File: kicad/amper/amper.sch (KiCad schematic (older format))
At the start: 59 parts, among them J1 Conn_02x05_Odd_Even, J2 Conn_02x05_Odd_Even, J3 Conn_02x05_Odd_Even, J4 USB_C_Receptacle_USB2.0, J5 Conn_01x03, J6 Conn_01x04, J7 Conn_01x05, J8 Conn_01x09, J9 Conn_01x09, Q1 FDS9435A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

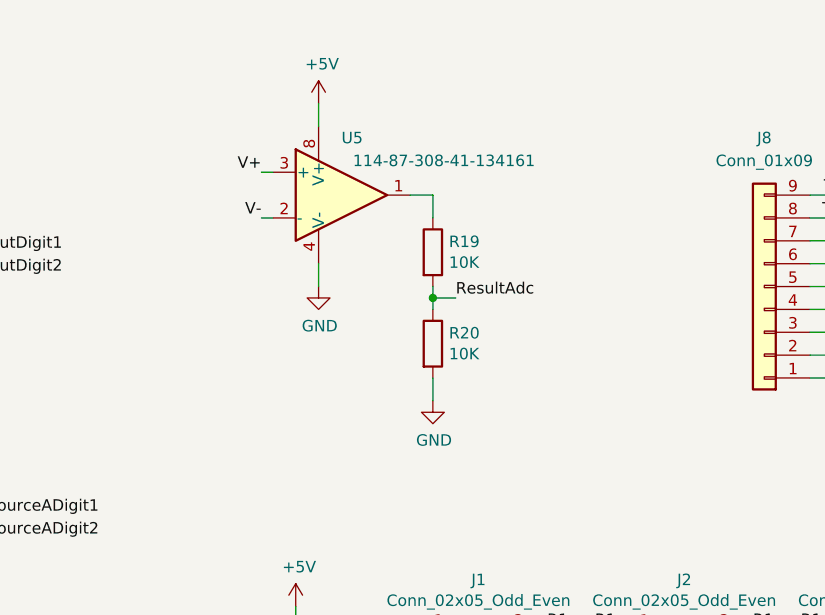
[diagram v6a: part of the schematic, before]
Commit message: high level schematic changes completed
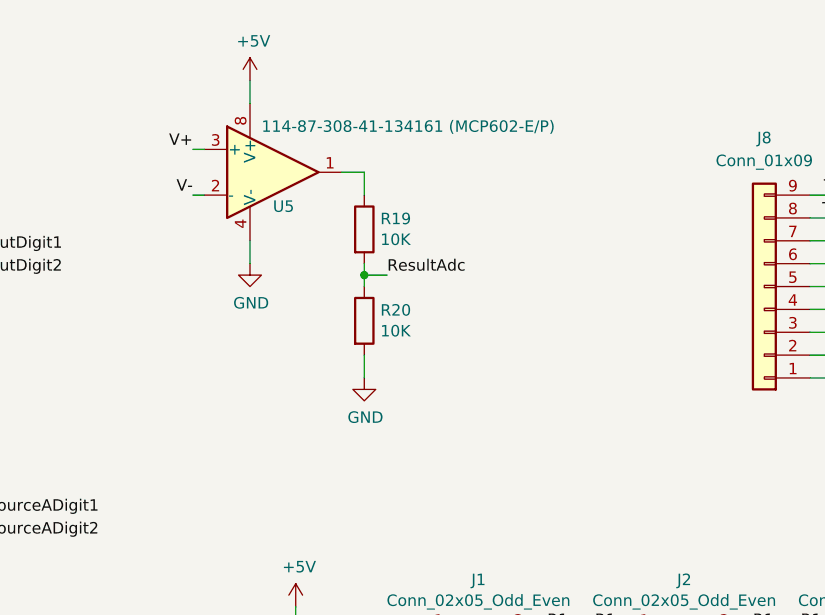
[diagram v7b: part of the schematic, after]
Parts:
- U5: value 114-87-308-41-134161 -> 114-87-308-41-134161 (MCP602-E/P)
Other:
- moved on the sheet: R19, R20, U5
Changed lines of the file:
@@
 Wire Wire Line
 	2000 7400 2350 7400
-Text Label 5150 1200 2    50   ~ 0
+Text Label 4850 1100 2    50   ~ 0
 V+
-Text Label 5150 1400 2    50   ~ 0
+Text Label 4850 1300 2    50   ~ 0
 V-
 Wire Wire Line
-	5800 1300 5900 1300
+	5500 1200 5600 1200
 Wire Wire Line
-	5400 900  5400 1000
+	5100 800  5100 900
 Wire Wire Line
-	5400 1600 5400 1700
+	5100 1500 5100 1600
 $Comp
 L power:+5V #PWR020
@@
 L amper-symbols:MCP602-single U5
 U 1 1 62259D5D
-P 5500 1300
-F 0 "U5" H 5500 1550 50  0000 L CNN
-F 1 "114-87-308-41-134161" H 5550 1450 50  0000 L CNN
-F 2 "amper:114-87-308-41-134161-generated" H 5550 1350 50  0001 C CNN
-F 3 "~" H 5650 1450 50  0001 C CNN
-F 4 "Not LCSC" H 5500 1300 50  0001 C CNN "Vendor"
-	1    5500 1300
+P 5200 1200
+F 0 "U5" H 5200 1050 50  0000 L CNN
+F 1 "114-87-308-41-134161 (MCP602-E/P)" H 5150 1400 50  0000 L CNN
+F 2 "amper:114-87-308-41-134161-generated" H 5250 1250 50  0001 C CNN
+F 3 "~" H 5350 1350 50  0001 C CNN
+F 4 "Not LCSC" H 5200 1200 50  0001 C CNN "Vendor"
+	1    5200 1200
 	1    0    0    -1
 $EndComp
-Text Label 6000 1750 0    50   ~ 0
+Text Label 5700 1650 0    50   ~ 0
 ResultAdc
 Wire Wire Line
-	5150 1400 5200 1400
+	4850 1300 4900 1300
 Wire Wire Line
-	5150 1200 5200 1200
+	4850 1100 4900 1100
 $Comp
 L power:GND #PWR09
 U 1 1 61CDCA7A
-P 5400 1700
-F 0 "#PWR09" H 5400 1450 50  0001 C CNN
-F 1 "GND" H 5405 1527 50  0000 C CNN
-F 2 "" H 5400 1700 50  0001 C CNN
-F 3 "~" H 5400 1700 50  0001 C CNN
-	1    5400 1700
+P 5100 1600
+F 0 "#PWR09" H 5100 1350 50  0001 C CNN
+F 1 "GND" H 5105 1427 50  0000 C CNN
+F 2 "" H 5100 1600 50  0001 C CNN
+F 3 "~" H 5100 1600 50  0001 C CNN
+	1    5100 1600
 	1    0    0    -1
 $EndComp
@@
 L power:+5V #PWR08
 U 1 1 61CC1B88
-P 5400 900
-F 0 "#PWR08" H 5400 750 50  0001 C CNN
-F 1 "+5V" H 5415 1073 50  0000 C CNN
-F 2 "" H 5400 900 50  0001 C CNN
-F 3 "~" H 5400 900 50  0001 C CNN
-	1    5400 900
+P 5100 800
+F 0 "#PWR08" H 5100 650 50  0001 C CNN
+F 1 "+5V" H 5115 973 50  0000 C CNN
+F 2 "" H 5100 800 50  0001 C CNN
+F 3 "~" H 5100 800 50  0001 C CNN
+	1    5100 800
 	1    0    0    -1
 $EndComp
@@
 L Device:R R19
 U 1 1 63215EE5
-P 5900 1550
-F 0 "R19" H 5970 1596 50  0000 L CNN
-F 1 "10K" H 5970 1505 50  0000 L CNN
-F 2 "Resistor_SMD:R_0603_1608Metric_Pad1.05x0.95mm_HandSolder" V 5830 1550 50  0001 C CNN
-F 3 "~" H 5900 1550 50  0001 C CNN
-	1    5900 1550
+P 5600 1450
+F 0 "R19" H 5670 1496 50  0000 L CNN
+F 1 "10K" H 5670 1405 50  0000 L CNN
+F 2 "Resistor_SMD:R_0603_1608Metric_Pad1.05x0.95mm_HandSolder" V 5530 1450 50  0001 C CNN
+F 3 "~" H 5600 1450 50  0001 C CNN
+	1    5600 1450
 	1    0    0    -1
 $EndComp
@@
 L Device:R R20
 U 1 1 632A6DD9
-P 5900 1950
-F 0 "R20" H 5970 1996 50  0000 L CNN
-F 1 "10K" H 5970 1905 50  0000 L CNN
-F 2 "Resistor_SMD:R_0603_1608Metric_Pad1.05x0.95mm_HandSolder" V 5830 1950 50  0001 C CNN
-F 3 "~" H 5900 1950 50  0001 C CNN
-	1    5900 1950
+P 5600 1850
+F 0 "R20" H 5670 1896 50  0000 L CNN
+F 1 "10K" H 5670 1805 50  0000 L CNN
+F 2 "Resistor_SMD:R_0603_1608Metric_Pad1.05x0.95mm_HandSolder" V 5530 1850 50  0001 C CNN
+F 3 "~" H 5600 1850 50  0001 C CNN
+	1    5600 1850
 	1    0    0    -1
 $EndComp
 Wire Wire Line
-	5900 1400 5900 1300
+	5600 1300 5600 1200
 Wire Wire Line
-	5900 1750 6000 1750
+	5600 1650 5700 1650
 Wire Wire Line
-	5900 1800 5900 1750
-Connection ~ 5900 1750
+	5600 1700 5600 1650
+Connection ~ 5600 1650
 Wire Wire Line
-	5900 1750 5900 1700
+	5600 1650 5600 1600
 $Comp
 L power:GND #PWR0106
 U 1 1 632FD6CD
-P 5900 2200
-F 0 "#PWR0106" H 5900 1950 50  0001 C CNN
-F 1 "GND" H 5905 2027 50  0000 C CNN
-F 2 "" H 5900 2200 50  0001 C CNN
-F 3 "~" H 5900 2200 50  0001 C CNN
-	1    5900 2200
+P 5600 2100
+F 0 "#PWR0106" H 5600 1850 50  0001 C CNN
+F 1 "GND" H 5605 1927 50  0000 C CNN
+F 2 "" H 5600 2100 50  0001 C CNN
+F 3 "~" H 5600 2100 50  0001 C CNN
+	1    5600 2100
 	1    0    0    -1
 $EndComp
 Wire Wire Line
-	5900 2100 5900 2200
+	5600 2000 5600 2100
 $EndSCHEMATC

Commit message: Rev C appears finished, going to sleep on it
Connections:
- net ResultAdc: no longer J1.9 (Pin_9), J7.5 (Pin_5)
- net SourceBAdc: now also J9.8 (Pin_8), U7.18 (PA2)
- net SourceBOut: no longer J9.8 (Pin_8), U7.18 (PA2)
- net ResultOut: now reaches R19.1, U5.1
- net ResultOut: now also J1.9 (Pin_9), J7.5 (Pin_5)
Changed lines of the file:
@@
 SourceAAdc
 Text Label 9300 1400 0    50   ~ 0
-SourceBOut
+SourceBAdc
 Text Label 9300 1300 0    50   ~ 0
 SourceAPwm
@@
 SourceBOut
 Text Label 10550 3400 2    50   ~ 0
-ResultAdc
+ResultOut
 Wire Wire Line
 	10550 3200 10650 3200
@@
 	5800 3600 5850 3600
 Text Label 5800 3600 2    50   ~ 0
-ResultAdc
+ResultOut
 Text Label 5800 3500 2    50   ~ 0
 SourceBOut
@@
 Wire Wire Line
 	5600 2000 5600 2100
+Text Label 5700 1200 0    50   ~ 0
+ResultOut
+Wire Wire Line
+	5600 1200 5700 1200
 $EndSCHEMATC
